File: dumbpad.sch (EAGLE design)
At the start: 40 parts

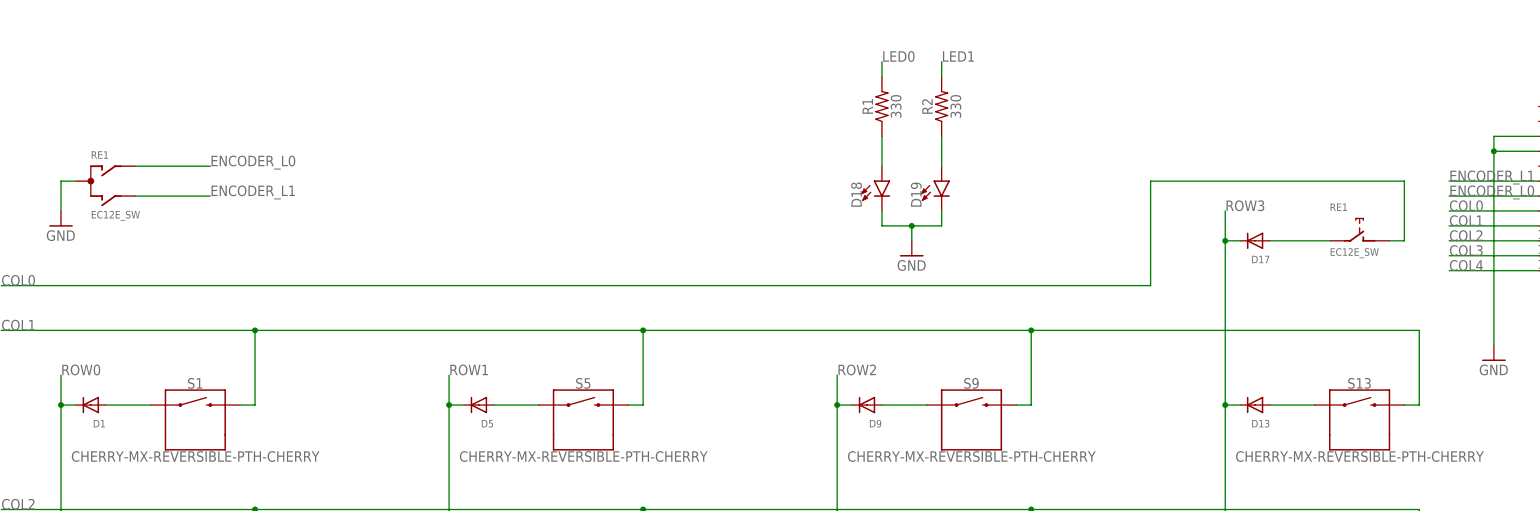
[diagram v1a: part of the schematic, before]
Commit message: added jumpers for reversing encoder when using encoder on right side instead of left
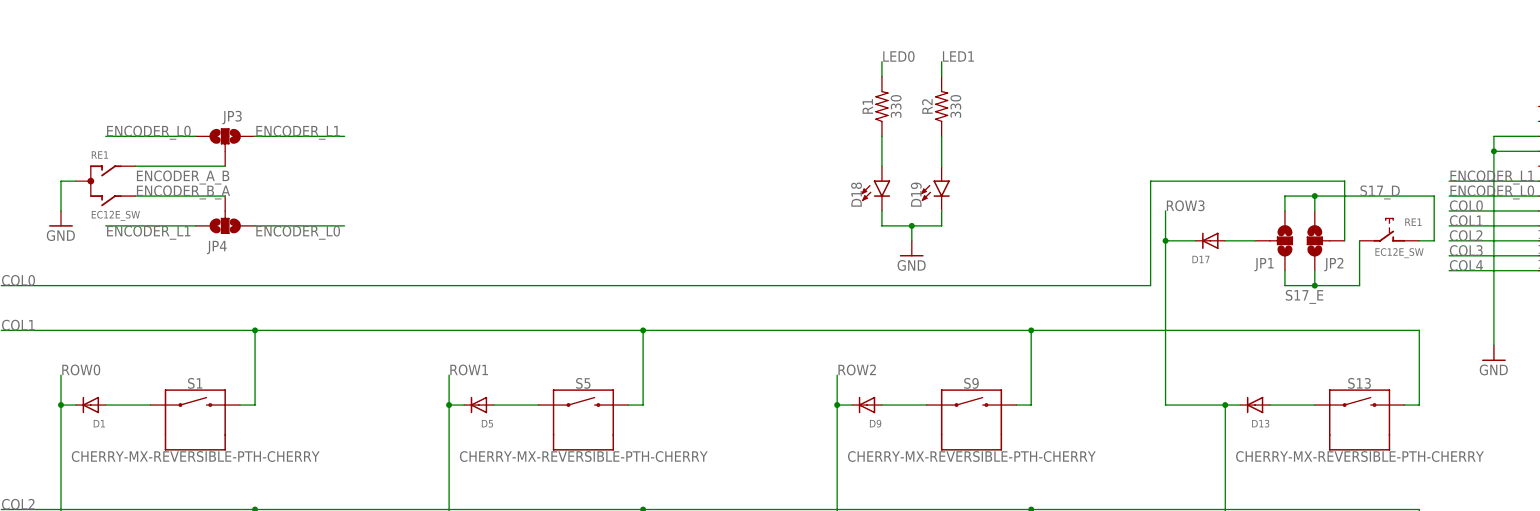
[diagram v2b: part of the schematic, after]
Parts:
- added JP1, JP2, JP3, JP4: JUMPER-SMT_3_NO_NO-SILK, SparkFun-Jumpers:JUMPER-SMT_3_NO_NO-SILK
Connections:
- removed net N$10: D17.A, RE1G$2.2
- new net ENCODER_A_B: JP3.2, RE1G$1.A
- new net ENCODER_B_A: JP4.2, RE1G$1.B
- new net ROW3_A: D17.A, JP1.2
- new net S17_D: JP1.1, JP2.3, RE1G$2.1
- new net S17_E: JP1.3, JP2.1, RE1G$2.2
- net COL0: now also JP2.2; no longer RE1G$2.1
- net ENCODER_L0: now also JP3.1, JP4.1; no longer RE1G$1.A
- net ENCODER_L1: now also JP3.3, JP4.3; no longer RE1G$1.B
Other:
- moved on the sheet: D17, RE1
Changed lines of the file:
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@@
 <?xml version="1.0" encoding="utf-8"?>
 <!DOCTYPE eagle SYSTEM "eagle.dtd">
-<eagle version="9.4.2">
+<eagle version="9.5.2">
 <drawing>
 <settings>
@@
 <setting verticaltext="up"/>
 </settings>
-<grid distance="0.1" unitdist="inch" unit="inch" style="lines" multiple="1" display="no" altdistance="0.01" altunitdist="inch" altunit="inch"/>
+<grid distance="0.1" unitdist="inch" unit="inch" style="lines" multiple="1" display="yes" altdistance="0.01" altunitdist="inch" altunit="inch"/>
 <layers>
 <layer number="1" name="Top" color="4" fill="1" visible="no" active="no"/>
@@
 <part name="S17" library="SparkFun-Switches" deviceset="MOMENTARY-SWITCH-SPST" device="-PTH-6.0MM"/>
 <part name="GND4" library="supply1" library_urn="urn:adsk.eagle:library:371" deviceset="GND" device=""/>
+<part name="JP1" library="SparkFun-Jumpers" deviceset="JUMPER-SMT_3_NO" device="_NO-SILK"/>
+<part name="JP2" library="SparkFun-Jumpers" deviceset="JUMPER-SMT_3_NO" device="_NO-SILK"/>
+<part name="JP3" library="SparkFun-Jumpers" deviceset="JUMPER-SMT_3_NO" device="_NO-SILK"/>
+<part name="JP4" library="SparkFun-Jumpers" deviceset="JUMPER-SMT_3_NO" device="_NO-SILK"/>
 </parts>
 <sheets>
@@
 <attribute name="VALUE" x="25.4" y="133.35" size="1.27" layer="96"/>
 </instance>
-<instance part="RE1" gate="G$2" x="241.3" y="129.54" smashed="yes">
-<attribute name="PART" x="236.22" y="134.62" size="1.27" layer="95"/>
-<attribute name="VALUE" x="236.22" y="127" size="1.27" layer="96"/>
+<instance part="RE1" gate="G$2" x="246.38" y="129.54" smashed="yes">
+<attribute name="PART" x="248.92" y="132.08" size="1.27" layer="95"/>
+<attribute name="VALUE" x="243.84" y="127" size="1.27" layer="96"/>
 </instance>
 <instance part="GND1" gate="1" x="20.32" y="132.08" smashed="yes">
@@
 <attribute name="VALUE" x="226.06" y="21.59" size="1.27" layer="96" rot="R180"/>
 </instance>
-<instance part="D17" gate="G$1" x="223.52" y="129.54" smashed="yes" rot="R180">
-<attribute name="NAME" x="226.06" y="127" size="1.27" layer="95" rot="R180"/>
-<attribute name="VALUE" x="226.06" y="133.35" size="1.27" layer="96" rot="R180"/>
+<instance part="D17" gate="G$1" x="215.9" y="129.54" smashed="yes" rot="R180">
+<attribute name="NAME" x="215.9" y="127" size="1.27" layer="95" rot="R180"/>
+<attribute name="VALUE" x="218.44" y="133.35" size="1.27" layer="96" rot="R180"/>
 </instance>
 <instance part="D18" gate="D1" x="160.02" y="139.7" smashed="yes">
@@
 <instance part="GND4" gate="1" x="287.02" y="66.04" smashed="yes">
 <attribute name="VALUE" x="284.48" y="63.5" size="1.778" layer="96"/>
+</instance>
+<instance part="JP1" gate="G$1" x="228.6" y="129.54" smashed="yes">
+<attribute name="NAME" x="223.52" y="124.841" size="1.778" layer="95" font="vector"/>
+</instance>
+<instance part="JP2" gate="G$1" x="233.68" y="129.54" smashed="yes" rot="R180">
+<attribute name="NAME" x="238.76" y="126.619" size="1.778" layer="95" font="vector" rot="R180"/>
+</instance>
+<instance part="JP3" gate="G$1" x="48.26" y="147.32" smashed="yes" rot="R90">
+<attribute name="NAME" x="47.879" y="149.86" size="1.778" layer="95" font="vector"/>
+</instance>
+<instance part="JP4" gate="G$1" x="48.26" y="132.08" smashed="yes" rot="R270">
+<attribute name="NAME" x="48.641" y="129.54" size="1.778" layer="95" font="vector" rot="R180"/>
 </instance>
 </instances>
@@
 <net name="ENCODER_L0" class="0">
 <segment>
-<pinref part="RE1" gate="G$1" pin="A"/>
-<wire x1="33.02" y1="142.24" x2="45.72" y2="142.24" width="0.1524" layer="91"/>
-<label x="45.72" y="142.24" size="1.778" layer="95"/>
-</segment>
-<segment>
 <pinref part="B1" gate="G$1" pin="4"/>
 <wire x1="271.78" y1="137.16" x2="256.54" y2="137.16" width="0.1524" layer="91"/>
 <label x="256.54" y="137.16" size="1.778" layer="95"/>
 </segment>
+<segment>
+<pinref part="JP3" gate="G$1" pin="1"/>
+<wire x1="43.18" y1="147.32" x2="27.94" y2="147.32" width="0.1524" layer="91"/>
+<label x="27.94" y="147.32" size="1.778" layer="95"/>
+</segment>
+<segment>
+<pinref part="JP4" gate="G$1" pin="1"/>
+<wire x1="53.34" y1="132.08" x2="68.58" y2="132.08" width="0.1524" layer="91"/>
+<label x="53.34" y="132.08" size="1.778" layer="95" align="top-left"/>
+</segment>
 </net>
 <net name="ENCODER_L1" class="0">
@@
 </segment>
 <segment>
-<pinref part="RE1" gate="G$1" pin="B"/>
-<wire x1="33.02" y1="137.16" x2="45.72" y2="137.16" width="0.1524" layer="91"/>
-<label x="45.72" y="137.16" size="1.778" layer="95"/>
+<pinref part="JP3" gate="G$1" pin="3"/>
+<wire x1="53.34" y1="147.32" x2="68.58" y2="147.32" width="0.1524" layer="91"/>
+<label x="53.34" y="147.32" size="1.778" layer="95"/>
+</segment>
+<segment>
+<pinref part="JP4" gate="G$1" pin="3"/>
+<wire x1="43.18" y1="132.08" x2="27.94" y2="132.08" width="0.1524" layer="91"/>
+<label x="27.94" y="132.08" size="1.778" layer="95" align="top-left"/>
 </segment>
 </net>
@@
 <wire x1="220.98" y1="45.72" x2="218.44" y2="45.72" width="0.1524" layer="91"/>
 <junction x="218.44" y="45.72"/>
-<label x="218.44" y="134.62" size="1.778" layer="95"/>
-<wire x1="218.44" y1="101.6" x2="218.44" y2="129.54" width="0.1524" layer="91"/>
+<label x="208.28" y="134.62" size="1.778" layer="95"/>
+<wire x1="218.44" y1="101.6" x2="208.28" y2="101.6" width="0.1524" layer="91"/>
+<wire x1="208.28" y1="101.6" x2="208.28" y2="129.54" width="0.1524" layer="91"/>
 <pinref part="D17" gate="G$1" pin="C"/>
-<wire x1="218.44" y1="129.54" x2="218.44" y2="134.62" width="0.1524" layer="91"/>
-<wire x1="220.98" y1="129.54" x2="218.44" y2="129.54" width="0.1524" layer="91"/>
-<junction x="218.44" y="129.54"/>
+<wire x1="208.28" y1="129.54" x2="208.28" y2="134.62" width="0.1524" layer="91"/>
+<wire x1="213.36" y1="129.54" x2="208.28" y2="129.54" width="0.1524" layer="91"/>
+<junction x="208.28" y="129.54"/>
 </segment>
 <segment>
@@
 <net name="COL0" class="0">
 <segment>
-<pinref part="RE1" gate="G$2" pin="1"/>
-<wire x1="246.38" y1="129.54" x2="248.92" y2="129.54" width="0.1524" layer="91"/>
-<wire x1="248.92" y1="129.54" x2="248.92" y2="139.7" width="0.1524" layer="91"/>
-<wire x1="248.92" y1="139.7" x2="205.74" y2="139.7" width="0.1524" layer="91"/>
 <label x="10.16" y="121.92" size="1.778" layer="95"/>
+<wire x1="238.76" y1="139.7" x2="205.74" y2="139.7" width="0.1524" layer="91"/>
 <wire x1="205.74" y1="139.7" x2="205.74" y2="121.92" width="0.1524" layer="91"/>
 <wire x1="205.74" y1="121.92" x2="10.16" y2="121.92" width="0.1524" layer="91"/>
+<pinref part="JP2" gate="G$1" pin="2"/>
+<wire x1="238.76" y1="139.7" x2="238.76" y2="129.54" width="0.1524" layer="91"/>
 </segment>
 <segment>
@@
 </segment>
 </net>
-<net name="N$10" class="0">
-<segment>
-<pinref part="D17" gate="G$1" pin="A"/>
-<pinref part="RE1" gate="G$2" pin="2"/>
-<wire x1="226.06" y1="129.54" x2="236.22" y2="129.54" width="0.1524" layer="91"/>
-</segment>
-</net>
 <net name="COL4" class="0">
 <segment>
@@
 <wire x1="294.64" y1="129.54" x2="302.26" y2="129.54" width="0.1524" layer="91"/>
 <label x="302.26" y="129.54" size="1.778" layer="95"/>
+</segment>
+</net>
+<net name="S17_E" class="0">
+<segment>
+<pinref part="JP1" gate="G$1" pin="3"/>
+<wire x1="228.6" y1="124.46" x2="228.6" y2="121.92" width="0.1524" layer="91"/>
+<wire x1="228.6" y1="121.92" x2="233.68" y2="121.92" width="0.1524" layer="91"/>
+<pinref part="RE1" gate="G$2" pin="2"/>
+<wire x1="233.68" y1="121.92" x2="241.3" y2="121.92" width="0.1524" layer="91"/>
+<wire x1="241.3" y1="121.92" x2="241.3" y2="129.54" width="0.1524" layer="91"/>
+<pinref part="JP2" gate="G$1" pin="1"/>
+<wire x1="233.68" y1="124.46" x2="233.68" y2="121.92" width="0.1524" layer="91"/>
+<junction x="233.68" y="121.92"/>
+<label x="228.6" y="119.38" size="1.778" layer="95"/>
+</segment>
+</net>
+<net name="S17_D" class="0">
+<segment>
+<pinref part="RE1" gate="G$2" pin="1"/>
+<wire x1="251.46" y1="129.54" x2="254" y2="129.54" width="0.1524" layer="91"/>
+<wire x1="254" y1="129.54" x2="254" y2="137.16" width="0.1524" layer="91"/>
+<wire x1="254" y1="137.16" x2="233.68" y2="137.16" width="0.1524" layer="91"/>
+<pinref part="JP1" gate="G$1" pin="1"/>
+<wire x1="233.68" y1="137.16" x2="228.6" y2="137.16" width="0.1524" layer="91"/>
+<wire x1="228.6" y1="134.62" x2="228.6" y2="137.16" width="0.1524" layer="91"/>
+<pinref part="JP2" gate="G$1" pin="3"/>
+<wire x1="233.68" y1="134.62" x2="233.68" y2="137.16" width="0.1524" layer="91"/>
+<junction x="233.68" y="137.16"/>
+<label x="241.3" y="137.16" size="1.778" layer="95"/>
+</segment>
+</net>
+<net name="ROW3_A" class="0">
+<segment>
+<pinref part="JP1" gate="G$1" pin="2"/>
+<pinref part="D17" gate="G$1" pin="A"/>
+<wire x1="218.44" y1="129.54" x2="223.52" y2="129.54" width="0.1524" layer="91"/>
+</segment>
+</net>
+<net name="ENCODER_A_B" class="0">
+<segment>
+<pinref part="RE1" gate="G$1" pin="A"/>
+<wire x1="33.02" y1="142.24" x2="48.26" y2="142.24" width="0.1524" layer="91"/>
+<label x="33.02" y="139.7" size="1.778" layer="95"/>
+<pinref part="JP3" gate="G$1" pin="2"/>
+</segment>
+</net>
+<net name="ENCODER_B_A" class="0">
+<segment>
+<pinref part="RE1" gate="G$1" pin="B"/>
+<wire x1="33.02" y1="137.16" x2="48.26" y2="137.16" width="0.1524" layer="91"/>
+<label x="33.02" y="137.16" size="1.778" layer="95"/>
+<pinref part="JP4" gate="G$1" pin="2"/>
 </segment>
 </net>
@@
 packages will not be understood (or retained) with this version.
 </note>
+<note version="9.0" severity="warning">
+Since Version 9.0, EAGLE supports the align property for labels.
+Labels in schematic will not be understood with this version. Update EAGLE to the latest version
+for full support of labels.
+</note>
 </compatibility>

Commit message: updated revision to v0.7
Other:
- note added: "Date: April 11, 2020"
- note added: "Rev: 0.7"
- note removed: "Date: August 29, 2019"
- note removed: "Rev: 0.6"
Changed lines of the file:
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@@
 <wire x1="0" y1="172.72" x2="0" y2="0" width="0.1524" layer="97"/>
 <text x="307.34" y="2.54" size="1.778" layer="97">Rev:
-0.6</text>
+0.7</text>
 <text x="279.4" y="2.54" size="1.778" layer="97">Date:
-August 29, 2019</text>
+April 11, 2020</text>
 <text x="279.4" y="10.16" size="1.778" layer="97">Design By:
 github.com/imchipwood</text>

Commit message: merging v08_jumpers to master
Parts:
- removed JP3, JP4: JUMPER-SMT_3_NO_NO-SILK, SparkFun-Jumpers:JUMPER-SMT_3_NO_NO-SILK
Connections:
- removed net ENCODER_A_B: JP3.2, RE1G$1.A
- removed net ENCODER_B_A: JP4.2, RE1G$1.B
- net ENCODER_L0: now also RE1G$1.A; no longer JP3.1, JP4.1
- net ENCODER_L1: now also RE1G$1.B; no longer JP3.3, JP4.3
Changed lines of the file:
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@@
 <setting verticaltext="up"/>
 </settings>
-<grid distance="0.1" unitdist="inch" unit="inch" style="lines" multiple="1" display="yes" altdistance="0.01" altunitdist="inch" altunit="inch"/>
+<grid distance="0.1" unitdist="inch" unit="inch" style="lines" multiple="1" display="no" altdistance="0.01" altunitdist="inch" altunit="inch"/>
 <layers>
 <layer number="1" name="Top" color="4" fill="1" visible="no" active="no"/>
@@
 <part name="JP1" library="SparkFun-Jumpers" deviceset="JUMPER-SMT_3_NO" device="_NO-SILK"/>
 <part name="JP2" library="SparkFun-Jumpers" deviceset="JUMPER-SMT_3_NO" device="_NO-SILK"/>
-<part name="JP3" library="SparkFun-Jumpers" deviceset="JUMPER-SMT_3_NO" device="_NO-SILK"/>
-<part name="JP4" library="SparkFun-Jumpers" deviceset="JUMPER-SMT_3_NO" device="_NO-SILK"/>
 </parts>
 <sheets>
@@
 <attribute name="NAME" x="238.76" y="126.619" size="1.778" layer="95" font="vector" rot="R180"/>
 </instance>
-<instance part="JP3" gate="G$1" x="48.26" y="147.32" smashed="yes" rot="R90">
-<attribute name="NAME" x="47.879" y="149.86" size="1.778" layer="95" font="vector"/>
-</instance>
-<instance part="JP4" gate="G$1" x="48.26" y="132.08" smashed="yes" rot="R270">
-<attribute name="NAME" x="48.641" y="129.54" size="1.778" layer="95" font="vector" rot="R180"/>
-</instance>
 </instances>
 <busses>
@@
 </segment>
 <segment>
-<pinref part="JP3" gate="G$1" pin="1"/>
-<wire x1="43.18" y1="147.32" x2="27.94" y2="147.32" width="0.1524" layer="91"/>
-<label x="27.94" y="147.32" size="1.778" layer="95"/>
-</segment>
-<segment>
-<pinref part="JP4" gate="G$1" pin="1"/>
-<wire x1="53.34" y1="132.08" x2="68.58" y2="132.08" width="0.1524" layer="91"/>
-<label x="53.34" y="132.08" size="1.778" layer="95" align="top-left"/>
+<pinref part="RE1" gate="G$1" pin="A"/>
+<wire x1="33.02" y1="142.24" x2="48.26" y2="142.24" width="0.1524" layer="91"/>
+<label x="33.02" y="142.24" size="1.778" layer="95"/>
 </segment>
 </net>
@@
 </segment>
 <segment>
-<pinref part="JP3" gate="G$1" pin="3"/>
-<wire x1="53.34" y1="147.32" x2="68.58" y2="147.32" width="0.1524" layer="91"/>
-<label x="53.34" y="147.32" size="1.778" layer="95"/>
-</segment>
-<segment>
-<pinref part="JP4" gate="G$1" pin="3"/>
-<wire x1="43.18" y1="132.08" x2="27.94" y2="132.08" width="0.1524" layer="91"/>
-<label x="27.94" y="132.08" size="1.778" layer="95" align="top-left"/>
+<pinref part="RE1" gate="G$1" pin="B"/>
+<wire x1="33.02" y1="137.16" x2="48.26" y2="137.16" width="0.1524" layer="91"/>
+<label x="33.02" y="137.16" size="1.778" layer="95"/>
 </segment>
 </net>
@@
 <pinref part="D17" gate="G$1" pin="A"/>
 <wire x1="218.44" y1="129.54" x2="223.52" y2="129.54" width="0.1524" layer="91"/>
-</segment>
-</net>
-<net name="ENCODER_A_B" class="0">
-<segment>
-<pinref part="RE1" gate="G$1" pin="A"/>
-<wire x1="33.02" y1="142.24" x2="48.26" y2="142.24" width="0.1524" layer="91"/>
-<label x="33.02" y="139.7" size="1.778" layer="95"/>
-<pinref part="JP3" gate="G$1" pin="2"/>
-</segment>
-</net>
-<net name="ENCODER_B_A" class="0">
-<segment>
-<pinref part="RE1" gate="G$1" pin="B"/>
-<wire x1="33.02" y1="137.16" x2="48.26" y2="137.16" width="0.1524" layer="91"/>
-<label x="33.02" y="137.16" size="1.778" layer="95"/>
-<pinref part="JP4" gate="G$1" pin="2"/>
 </segment>
 </net>
@@
 packages will not be understood (or retained) with this version.
 </note>
-<note version="9.0" severity="warning">
-Since Version 9.0, EAGLE supports the align property for labels.
-Labels in schematic will not be understood with this version. Update EAGLE to the latest version
-for full support of labels.
-</note>
 </compatibility>
